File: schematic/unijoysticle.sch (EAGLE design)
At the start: 8 parts, among them IC1 4066N, IC2 4066N, IC3 4066N, J1 DB9, J2 DB9, J3 POWER_JACKSLT

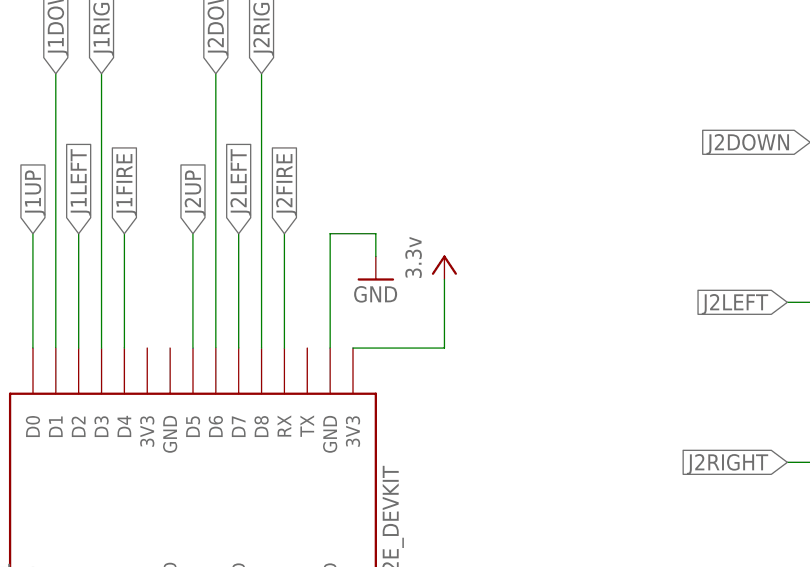
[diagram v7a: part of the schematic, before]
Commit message: fix: schematic doesn't use ESP8266 VCC
and uses Copper Pour
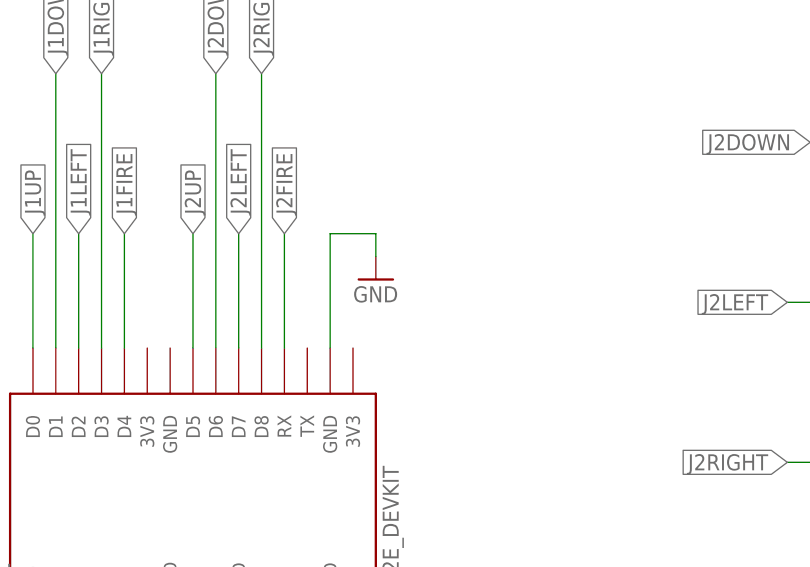
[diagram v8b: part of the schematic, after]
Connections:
- net VCC: no longer MOD1.3V3@2
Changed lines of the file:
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@@
 <attributes>
 <attribute name="CNAME" value="Retro Moe"/>
-<attribute name="CREVISION" value="0.2.1"/>
+<attribute name="CREVISION" value="0.2.2"/>
 <attribute name="DESIGNER" value="Ricardo Quesada"/>
 </attributes>
@@
 <part name="GND3" library="supply1" deviceset="GND" device=""/>
 <part name="GND4" library="supply1" deviceset="GND" device=""/>
-<part name="P+1" library="supply1" deviceset="VCC" device="" value="3.3v"/>
 <part name="IC2" library="40xx" deviceset="4066" device="N">
 <attribute name="MF" value="TEXAS INSTRUMENTS"/>
@@
 <instance part="GND3" gate="1" x="149.86" y="86.36"/>
 <instance part="GND4" gate="1" x="101.6" y="124.46"/>
-<instance part="P+1" gate="VCC" x="157.48" y="88.9"/>
 <instance part="IC2" gate="A" x="53.34" y="53.34">
 <attribute name="OC_NEWARK" x="53.34" y="53.34" size="1.778" layer="96" display="off"/>
@@
 <net name="VCC" class="0">
 <segment>
-<pinref part="P+1" gate="VCC" pin="VCC"/>
-<wire x1="147.32" y1="78.74" x2="157.48" y2="78.74" width="0.1524" layer="91"/>
-<wire x1="157.48" y1="78.74" x2="157.48" y2="86.36" width="0.1524" layer="91"/>
-<pinref part="MOD1" gate="G$1" pin="3V3@2"/>
-</segment>
-<segment>
 <pinref part="J2" gate="G$1" pin="7"/>
